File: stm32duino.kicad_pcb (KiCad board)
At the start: 2 copper layers, 87.6 x 48.3 mm, 19 parts, among them P1 CONN_02X07, P2 CONN_01X04, P3 DISP_SER, P4 HOST_SER, U1 stm32f103c8t6-module-china

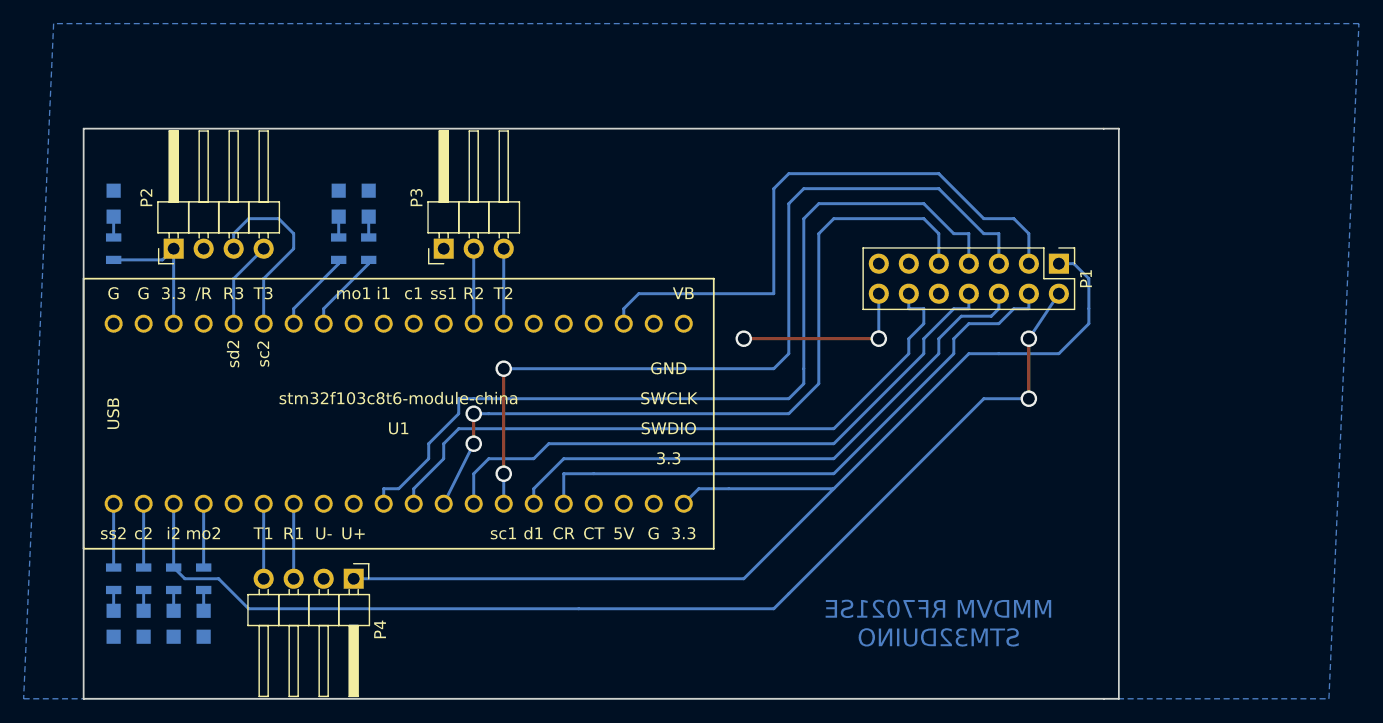
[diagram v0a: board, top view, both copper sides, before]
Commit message: Minor beautification, added OSHW logo to PCB
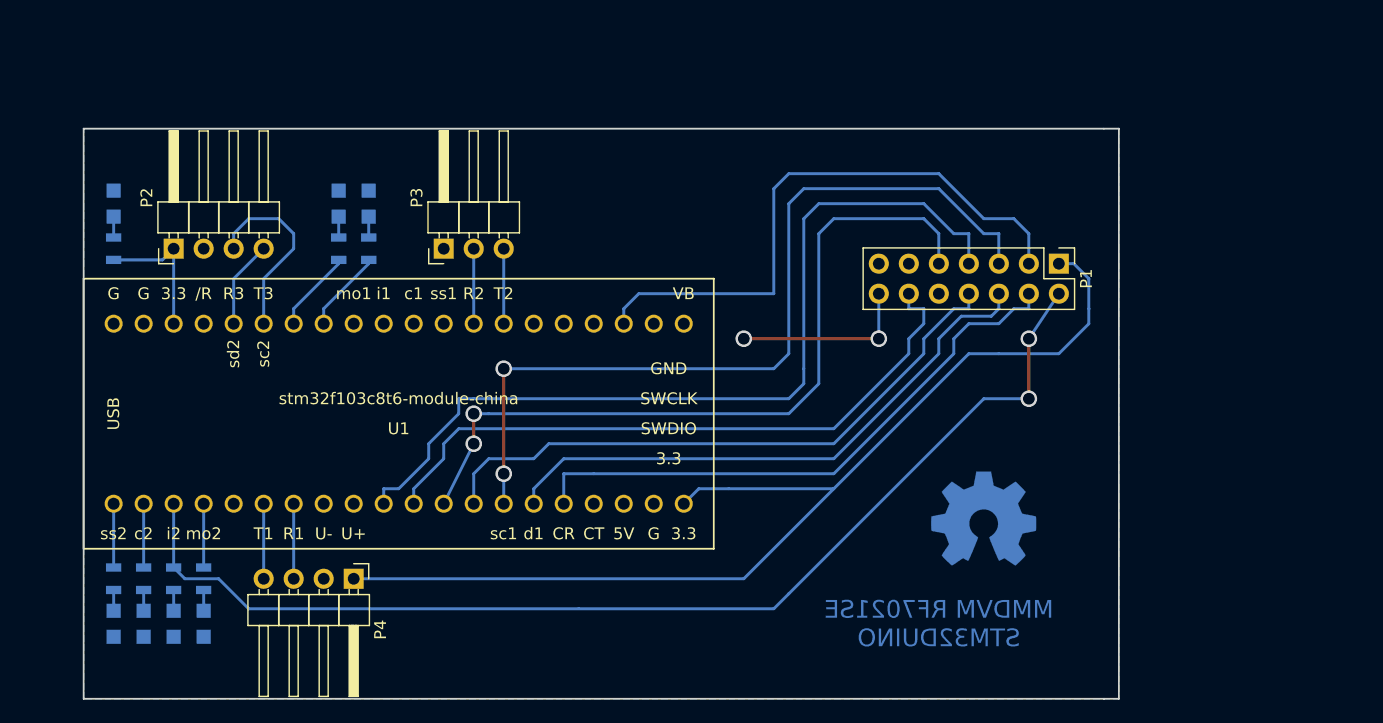
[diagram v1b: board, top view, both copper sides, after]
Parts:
- added REF***: OSHW-Symbol_8.9x8mm_Copper, Symbols:OSHW-Symbol_8.9x8mm_Copper, B.Cu at (176.5, 68.6)

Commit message: Added placement and schematic pdf
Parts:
- P1: value CONN_02X07 -> RF7021SE
- P2: value CONN_01X04 -> DISP_I2C
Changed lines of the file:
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@@
     (links 47)
     (no_connects 1)
-    (area 74.700001 26.67 208.280001 99.220001)
+    (area 100.254999 35.484999 188.035001 83.895001)
     (thickness 1.6)
     (drawings 12)
@@
     (pad_to_mask_clearance 0.2)
     (aux_axis_origin 0 0)
-    (visible_elements 7FFFFFFF)
+    (visible_elements 7FFFEFFF)
     (pcbplotparams
       (layerselection 0x00030_80000001)
@@
       (effects (font (size 1 1) (thickness 0.15)))
     )
-    (fp_text value CONN_01X04 (at 4.315 9.89 90) (layer F.Fab)
+    (fp_text value DISP_I2C (at 4.315 9.89 90) (layer F.Fab)
       (effects (font (size 1 1) (thickness 0.15)))
     )
@@
       (effects (font (size 1 1) (thickness 0.15)))
     )
-    (fp_text value CONN_02X07 (at 1.27 17.57 270) (layer F.Fab)
-      (effects (font (size 1 1) (thickness 0.15)))
-    )
+    (fp_text value RF7021SE (at 1.27 17.57 270) (layer F.Fab)
+      (effects (font (size 1 1) (thickness 0.15)))
+    )
